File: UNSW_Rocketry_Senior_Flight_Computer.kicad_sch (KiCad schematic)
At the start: 0 parts

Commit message: starting work
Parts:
- added C1, C10, C2, C3, C7, C8: 0.1uF, PCM_SparkFun-Capacitor:C_0603_1608Metric, symbol PCM_SparkFun-Capacitor:0.1uF_0603_25V_20%
- added C4: 4.7uF, PCM_SparkFun-Capacitor:C_0603_1608Metric, symbol PCM_SparkFun-Capacitor:4.7uF_0603_35V_20%
- added C5, C9: 1.0uF, PCM_SparkFun-Capacitor:C_0603_1608Metric, symbol PCM_SparkFun-Capacitor:1.0uF_0603_16V_10%
- added C6: 10nF, PCM_SparkFun-Capacitor:C_0603_1608Metric, symbol PCM_SparkFun-Capacitor:10nF_0603_50V_10%
- added U1: STM32L452RETx, Package_QFP:LQFP-64_10x10mm_P0.5mm, symbol MCU_ST_STM32L4:STM32L452RETx
- added U2, U3: MS5611-01BA, Package_LGA:LGA-8_3x5mm_P1.25mm, symbol Sensor_Pressure:MS5611-01BA
- added U4: LIS3DH, Package_LGA:LGA-16_3x3mm_P0.5mm_LayoutBorder3x5y, symbol Sensor_Motion:LIS3DH
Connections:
- new net: U2.4 (CSB), U2.5 (CSB)
- new net: U4.10 (GND), U4.12 (GND), U4.5 (GND)
- new net: U3.4 (CSB), U3.5 (CSB)
- new net +3.3V: C1.2, C10.1, C2.2, C3.2, C4.2, C5.1, C6.2, C7.2, C8.1, C9.2, U1.1 (VBAT), U1.13 (VDDA), U1.19 (VDD), U1.32 (VDD), U1.48 (VDDUSB), U1.64 (VDD)
- new net GND: C1.1, C10.2, C2.1, C3.1, C4.1, C5.2, C6.1, C7.1, C8.2, C9.1, U1.12 (VSSA), U1.18 (VSS), U1.31 (VSS), U1.47 (VSS), U1.63 (VSS)

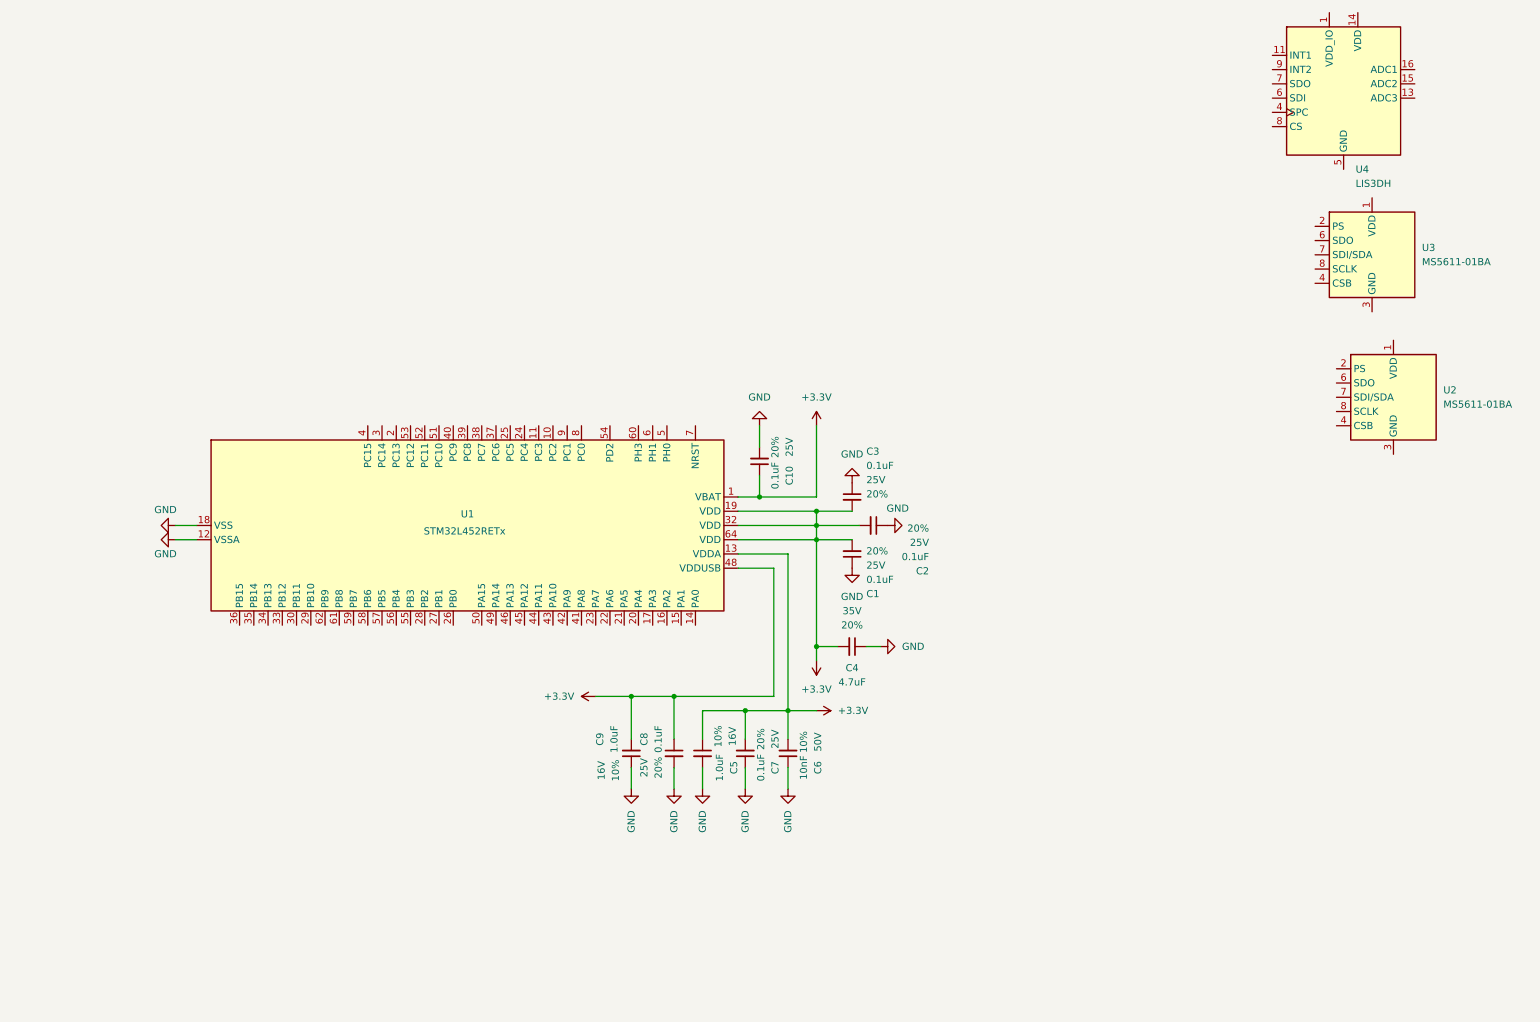
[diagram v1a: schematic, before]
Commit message: feat: MCU setup
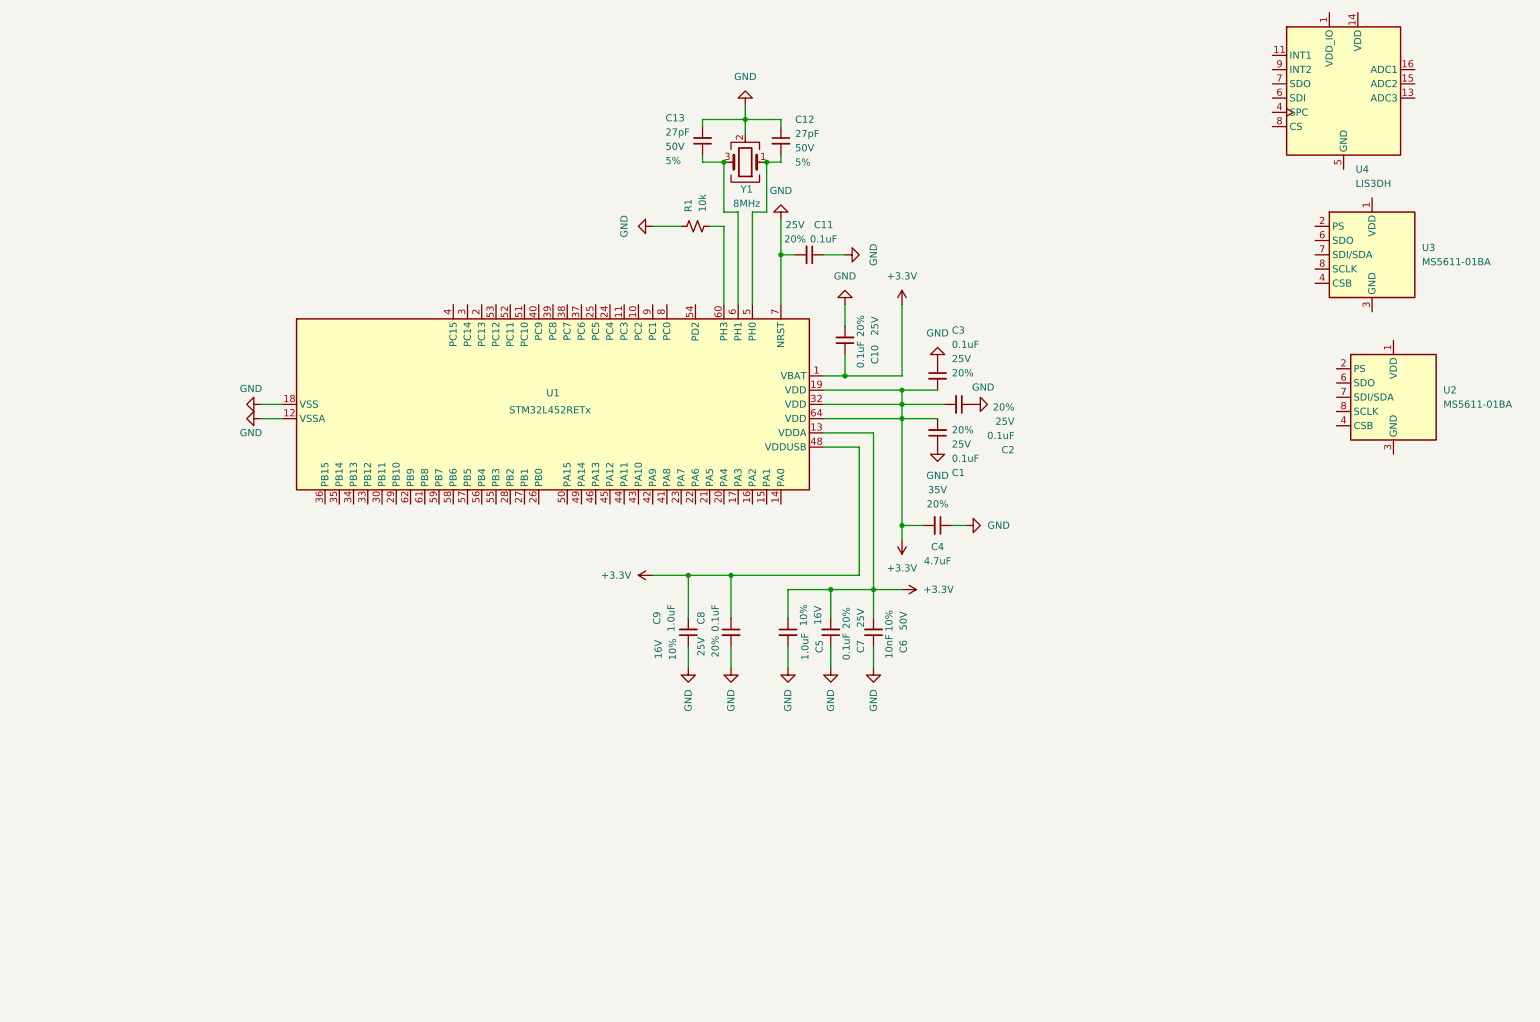
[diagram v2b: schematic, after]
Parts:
- added C11: 0.1uF, PCM_SparkFun-Capacitor:C_0603_1608Metric, symbol PCM_SparkFun-Capacitor:0.1uF_0603_25V_20%
- added C12, C13: 27pF, PCM_SparkFun-Capacitor:C_0603_1608Metric, symbol PCM_SparkFun-Capacitor:27pF_0603_50V_5%
- added R1: 10k, PCM_SparkFun-Resistor:R_0603_1608Metric, symbol PCM_SparkFun-Resistor:10k_0603
- added Y1: 8MHz, Crystal:Crystal_SMD_3225-4Pin_3.2x2.5mm_HandSoldering, symbol Device:Crystal_GND24
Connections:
- net GND: now also U1.7 (NRST), C11.1, C11.2, C12.1, C13.2, R1.2, Y1.2 (G), Y1.4 (G)
- net at U1.5 (PH0): now also C12.2, Y1.1
- net at U1.6 (PH1): now also C13.1, Y1.3
- net at U1.60 (PH3): now also R1.1
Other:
- moved on the sheet: C1, C10, C2, C3, C4, C5, C6, C7, C8, C9, U1

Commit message: feat: Power & comms
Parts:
- removed U2, U3: MS5611-01BA, Package_LGA:LGA-8_3x5mm_P1.25mm, symbol Sensor_Pressure:MS5611-01BA
- removed U4: LIS3DH, Package_LGA:LGA-16_3x3mm_P0.5mm_LayoutBorder3x5y, symbol Sensor_Motion:LIS3DH
- added J1: SWD, Connector_PinHeader_2.54mm:PinHeader_1x05_P2.54mm_Vertical, symbol Connector:Conn_01x05_Pin
- added SW1: SW_Push, Button_Switch_SMD:SW_SPST_PTS645Sx43SMTR92, symbol Switch:SW_Push
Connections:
- net +3.3V: now also J1.1 (Pin_1)
- net GND: now also J1.4 (Pin_4), SW1.2; no longer C11.2, U1.7 (NRST)
- net INT2_LIS3DH: now reaches U1.10 (PC2)
- net SD_CD: now reaches U1.11 (PC3)
- net SPI1_MISO: now reaches U1.22 (PA6)
- net SPI1_MOSI: now reaches U1.23 (PA7)
- net CS_H3LIS: now reaches U1.26 (PB0)
- net CS_LIS3DH: now reaches U1.27 (PB1)
- net CS_MS5611_1: now reaches U1.28 (PB2)
- net CS_MS5611_2: now reaches U1.33 (PB12)
- net SDMMC_D0: now reaches U1.39 (PC8)
- net SDMMC_D1: now reaches U1.40 (PC9)
- net SPI1_SCK: now reaches U1.41 (PA8)
- net SWDIO: now reaches U1.46 (PA13)
- net SWDIO: now also J1.2 (Pin_2)
- net SWCLK: now reaches U1.49 (PA14)
- net SWCLK: now also J1.3 (Pin_3)
- net SDMMC_D2: now reaches U1.51 (PC10)
- net SDMMC_D3: now reaches U1.52 (PC11)
- net SDMMC_CLK: now reaches U1.53 (PC12)
- net SDMMC_CMD: now reaches U1.54 (PD2)
- net INT1_H3LIS: now reaches U1.8 (PC0)
- net INT1_LIS3DH: now reaches U1.9 (PC1)
- new net NRST: C11.2, J1.5 (Pin_5), SW1.1, U1.7 (NRST)
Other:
- added sheet Comms (Comms.kicad_sch)
- added sheet Peripherals (Peripherals.kicad_sch)
- added sheet Power (Power.kicad_sch)
- moved on the sheet: C1, C10, C11, C12, C13, C2, C3, C4, C5, C6, C7, C8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

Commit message: feat: Comms complete
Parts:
- removed J1: SWD, Connector_PinHeader_2.54mm:PinHeader_1x05_P2.54mm_Vertical, symbol Connector:Conn_01x05_Pin
- removed SW1: SW_Push, Button_Switch_SMD:SW_SPST_PTS645Sx43SMTR92, symbol Switch:SW_Push
- added JP1: RESET_JMP, TestPoint:TestPoint_2Pads_Pitch2.54mm_Drill0.8mm, symbol Jumper:Jumper_2_Open
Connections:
- net GND: now also JP1.2 (B)
- net NRST: now also JP1.1 (A)
- net UART_TX: now reaches U1.16 (PA2)
- net UART_RX: now reaches U1.17 (PA3)
- net USB_N: now reaches U1.44 (PA11)
- net USB_P: now reaches U1.45 (PA12)

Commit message: feat: Pyro done
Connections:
- net PYRO1_CONT: now reaches U1.14 (PA0)
- net PYRO2_CONT: now reaches U1.15 (PA1)
- net PYRO_BATT_SENSE: now reaches U1.20 (PA4)
- net PYRO1_CONT_LED: now reaches U1.29 (PB10)
- net PYRO2_CONT_LED: now reaches U1.30 (PB11)
- net PYRO_ARM: now reaches U1.34 (PB13)
- net PYRO1_GATE: now reaches U1.35 (PB14)
- net PYRO2_GATE: now reaches U1.36 (PB15)
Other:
- added sheet Pyros (Pyros.kicad_sch)

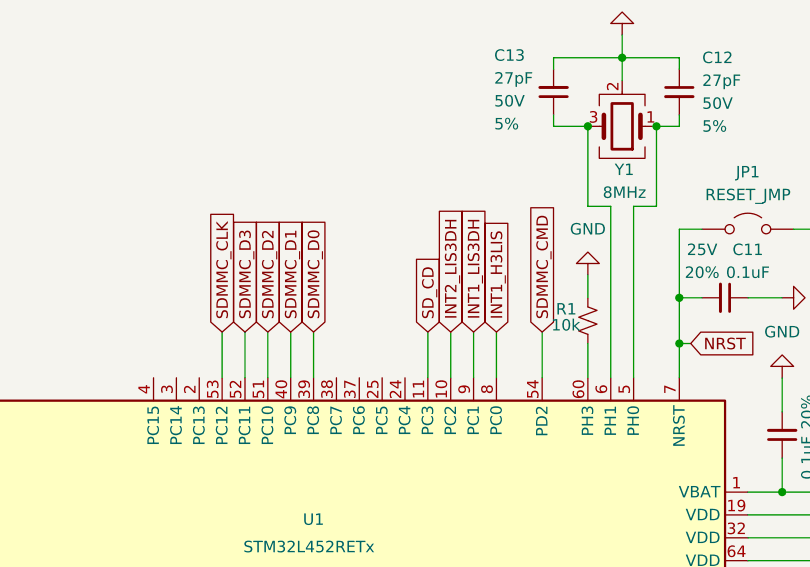
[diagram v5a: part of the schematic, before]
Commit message: feat: VBAT Sense
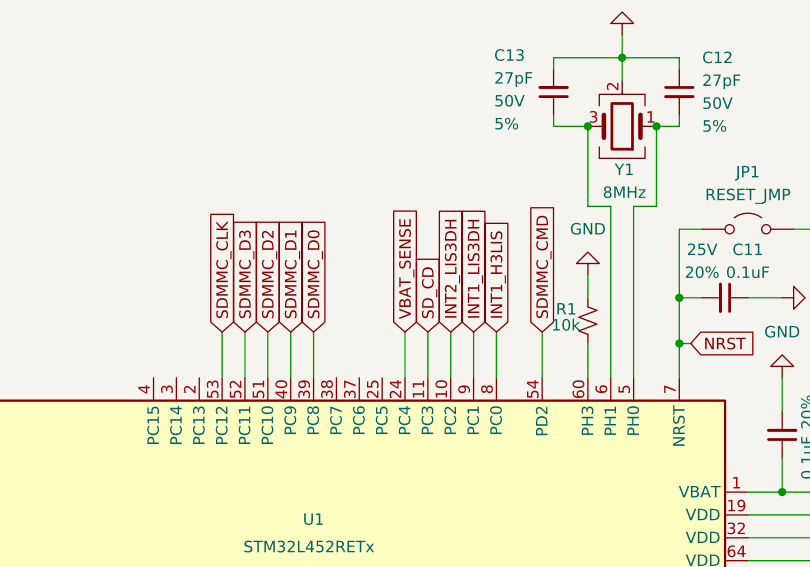
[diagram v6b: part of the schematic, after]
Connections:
- net VBAT_SENSE: now reaches U1.24 (PC4)
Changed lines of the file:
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@@
+	(wire
+		(pts
+			(xy 146.05 66.04) (xy 146.05 71.12)
+		)
+		(stroke
+			(width 0)
+			(type default)
+		)
+	)
 	(wire
 		(pts
@@
 			)
 		)
+	)
+	(global_label "VBAT_SENSE"
+		(shape input)
+		(at 146.05 66.04 90)
+		(fields_autoplaced yes)
+		(effects
+			(font
+				(size 1.27 1.27)
+			)
+			(justify left)
+		)
+		(property "Intersheetrefs" "${INTERSHEET_REFS}"
+			(at 146.05 51.6249 90)
+			(hide yes)
+			(show_name no)
+			(do_not_autoplace no)
+			(effects
+				(font
+					(size 1.27 1.27)
+				)
+				(justify left)
+			)
+		)

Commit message: feat: finish board (draft)
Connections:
- net SPI1_SCK: now also U1.21 (PA5); no longer U1.41 (PA8)
- net RGB_G: now reaches U1.42 (PA9)
- net RGB_B: now reaches U1.43 (PA10)
- net LED_HEARTBEAT: now reaches U1.58 (PB6)
- net LED_ERROR: now reaches U1.59 (PB7)
- net PG_BUCKBOOST: now reaches U1.61 (PB8)
- net BUZZER: now reaches U1.62 (PB9)
- new net RGB_R: U1.41 (PA8)
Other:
- added sheet Indication (Indication.kicad_sch)

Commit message: feat: finish schematic (erc_pass)
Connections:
- no-connect marks 0 -> 10
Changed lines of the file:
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@@
 		(color 0 0 0 0)
+	)
+	(no_connect
+		(at 138.43 71.12)
+	)
+	(no_connect
+		(at 125.73 106.68)
+	)
+	(no_connect
+		(at 143.51 71.12)
+	)
+	(no_connect
+		(at 138.43 106.68)
+	)
+	(no_connect
+		(at 123.19 106.68)
+	)
+	(no_connect
+		(at 120.65 71.12)
+	)
+	(no_connect
+		(at 120.65 106.68)
+	)
+	(no_connect
+		(at 118.11 71.12)
+	)
+	(no_connect
+		(at 140.97 71.12)
+	)
+	(no_connect
+		(at 123.19 71.12)
 	)
 	(wire
